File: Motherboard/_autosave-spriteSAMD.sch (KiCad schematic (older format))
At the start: 39 parts, among them IC1 BMX160, J1 Conn_01x01, J2 10118194-0001LF, J28 Conn_01x01, J29 Conn_01x01, J3 Micro_SD_Card, J30 Conn_01x01, J4 xf2m-2415-1a, J5 XF2M-1015-1A, SW1 KMR231NG LFS, U1 RFM95W-915S2, U2 ATSAMD51G_TQFN48, U3 DRV8833PWP, U4 TPS82740BSIPR, U5 DRV8833PWP, U6 MAX708RESA-T, U8 RFM95W-915S2, X1 ANTENNA_U.FL, X2 ANTENNA_U.FL

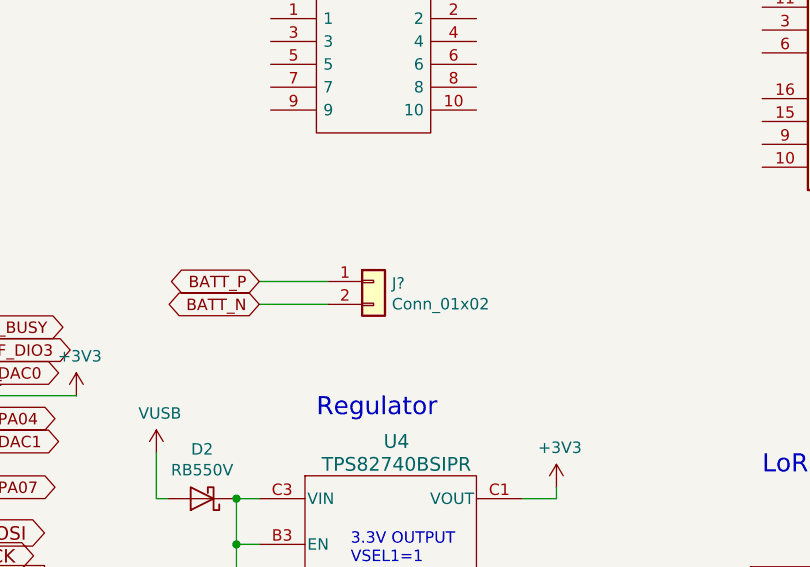
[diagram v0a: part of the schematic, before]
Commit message: added WDT and took closer-look at fit
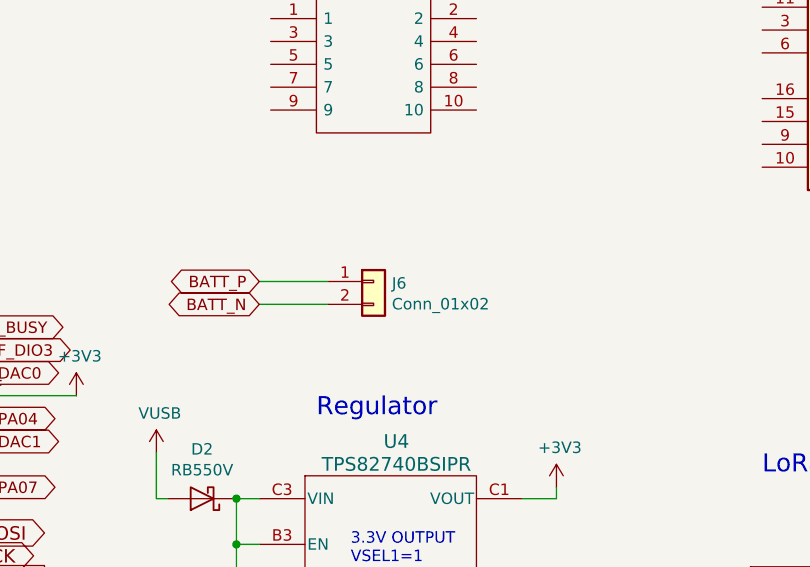
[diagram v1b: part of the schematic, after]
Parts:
- gave numbers to parts that had none: 1
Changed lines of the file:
@@
 ~RESET
 $Comp
-L Connector_Generic:Conn_01x02 J?
+L Connector_Generic:Conn_01x02 J6
 U 1 1 5DB0C730
 P 6300 3800
-F 0 "J?" H 6380 3792 50  0000 L CNN
+F 0 "J6" H 6380 3792 50  0000 L CNN
 F 1 "Conn_01x02" H 6380 3701 50  0000 L CNN
 F 2 "Connector_PinHeader_2.54mm:PinHeader_1x02_P2.54mm_Vertical" H 6300 3800 50  0001 C CNN
